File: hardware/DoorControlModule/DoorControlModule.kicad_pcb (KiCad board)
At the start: 6 copper layers, 68.5 x 65.5 mm, 135 parts, among them IC1 CY8C4147AZE-S475, IC2 TLS850B0TBV33ATMA1, IC3 TJA1043T,118, IC4 MAX6818, IC5 LM2901BYPT, IC6 BTS72002EPAXUMA1, IC7 LM74610, J1 501331-0507, J2 64334-0100, Q1 VOMA618A-4X001T, Q2 VOMA618A-4X001T, Q3 IPD50N04S4L08ATMA1, U0 BTM9021EP, U1 BTM9021EP, U2 BTM9021EP, U3 BTN70301EPAXUMA1, U4 BTN70301EPAXUMA1, U5 BTN70301EPAXUMA1, U6 BTN9990LV, U7 BTN9990LV, Y1 CX3225CA24000D0HSSCC, Y2 NX3215SA-32.768K-STD-MUS-2

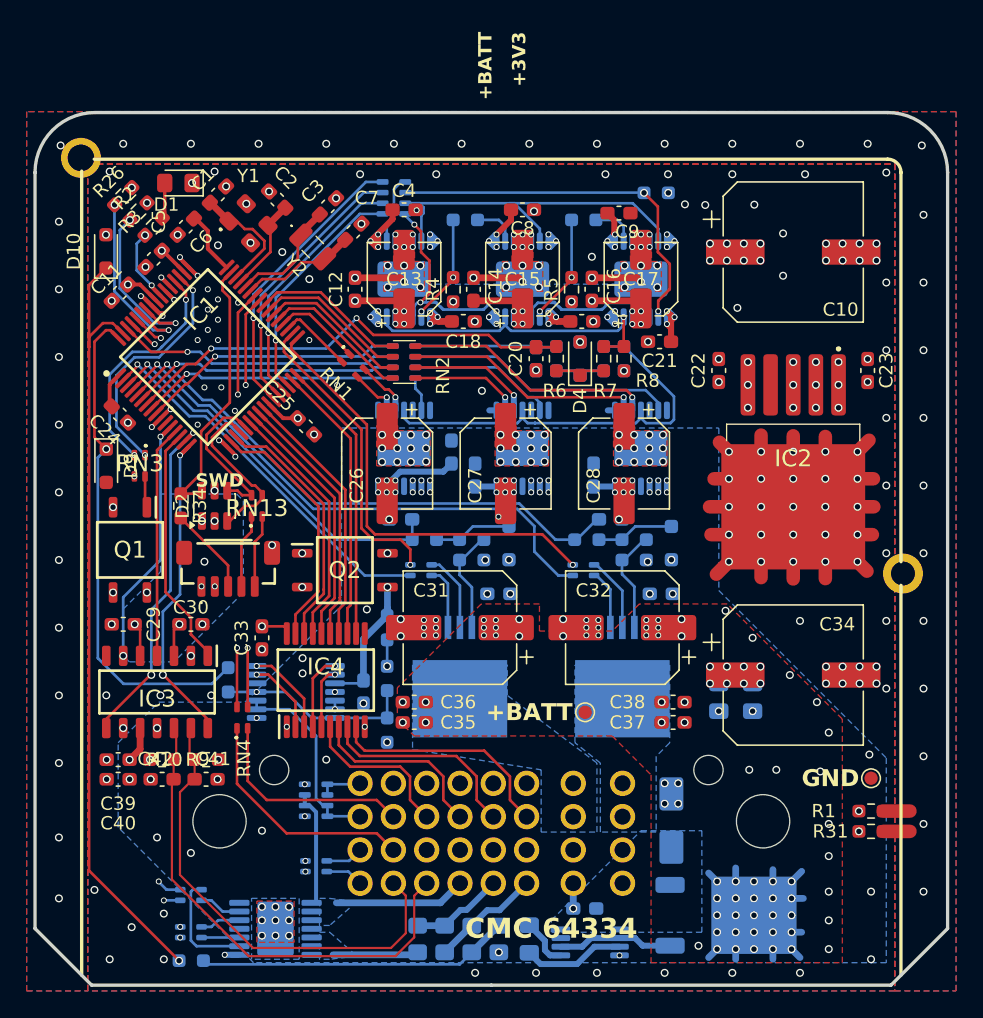
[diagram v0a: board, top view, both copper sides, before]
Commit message: teardrops added, pcb footprint refreshed
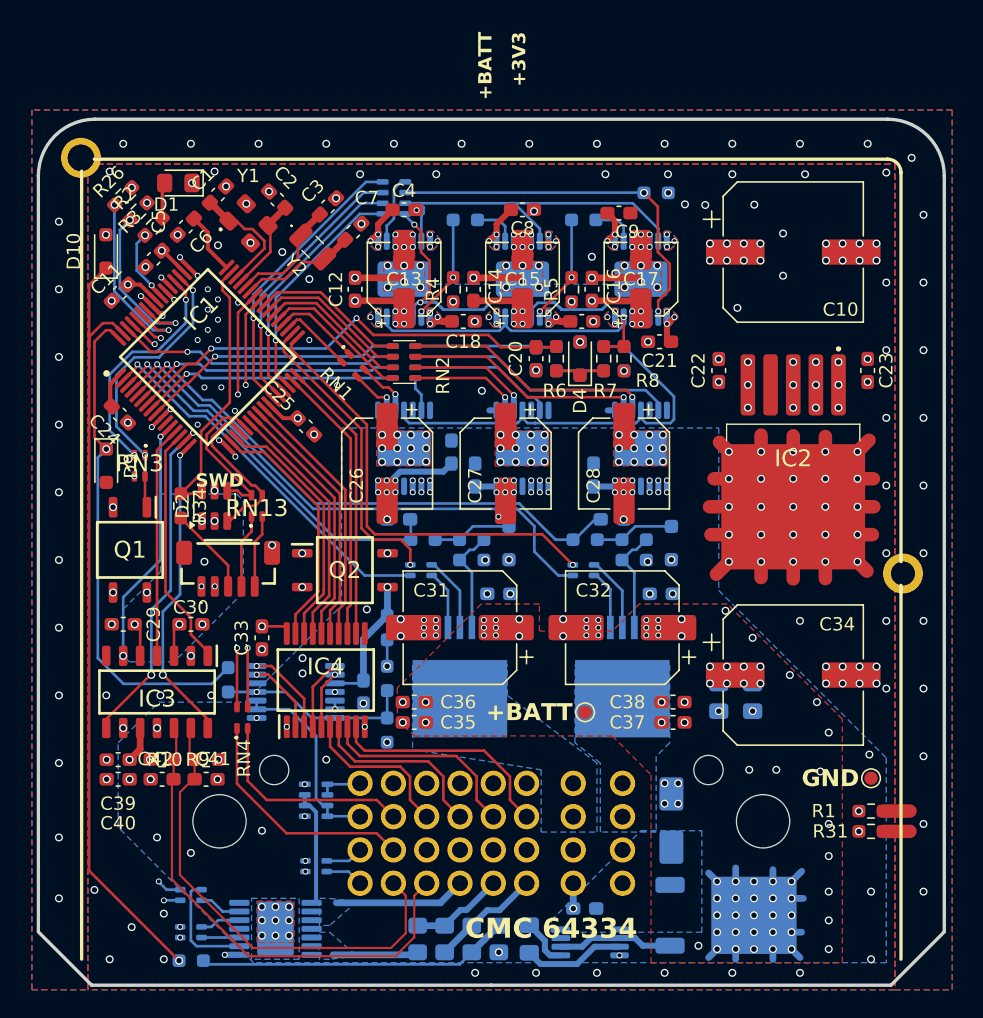
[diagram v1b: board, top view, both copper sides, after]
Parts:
- moved J2 49.8 mm to (137.0, 80.8)
- moved C48 0.15 mm to (129.9, 81.8)
- moved C47 0.13 mm to (145.9, 81.8)
- moved R19 0.13 mm to (143.9, 83.3)
- moved R22 0.10 mm to (131.7, 83.3)
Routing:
- net door_lock_motor_lock: track 59.2 -> 51.4 mm
- net mirror_motor_down: track 53.6 -> 48.5 mm
- net mirror_motor_right: track 51.3 -> 46.4 mm
- net h_bridge_b: track 51.4 -> 46.9 mm
- net door_lock_motor_unlock: track 54.5 -> 51.1 mm
- net h_bridge_a: track 52.0 -> 48.5 mm
- net Earth: vias 36 -> 35
- added copper zone on B.Cu, net door_lock_motor_lock
- added copper zone on F.Cu, net door_lock_motor_lock
- added copper zone on B.Cu, net door_lock_motor_unlock
- added copper zone on F.Cu, net door_lock_motor_unlock
- added copper zone on B.Cu, net h_bridge_a
- added copper zone on F.Cu, net h_bridge_a
- added copper zone on B.Cu, net h_bridge_b
- added copper zone on F.Cu, net h_bridge_b
- added copper zone on B.Cu, net mirror_motor_down
- added copper zone on F.Cu, net mirror_motor_down
- added copper zone on B.Cu, net mirror_motor_right
- added copper zone on F.Cu, net mirror_motor_right
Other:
- board size 68.5 x 65.5 mm -> 68 x 65 mm
